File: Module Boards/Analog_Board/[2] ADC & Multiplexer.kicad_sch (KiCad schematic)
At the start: 10 parts, among them J1 212134-0003, J2 212134-0003, J3 212134-0003, J4 212134-0003, U1 LTC1864LIMS8#PBF, U5 TMUX1104DQAR

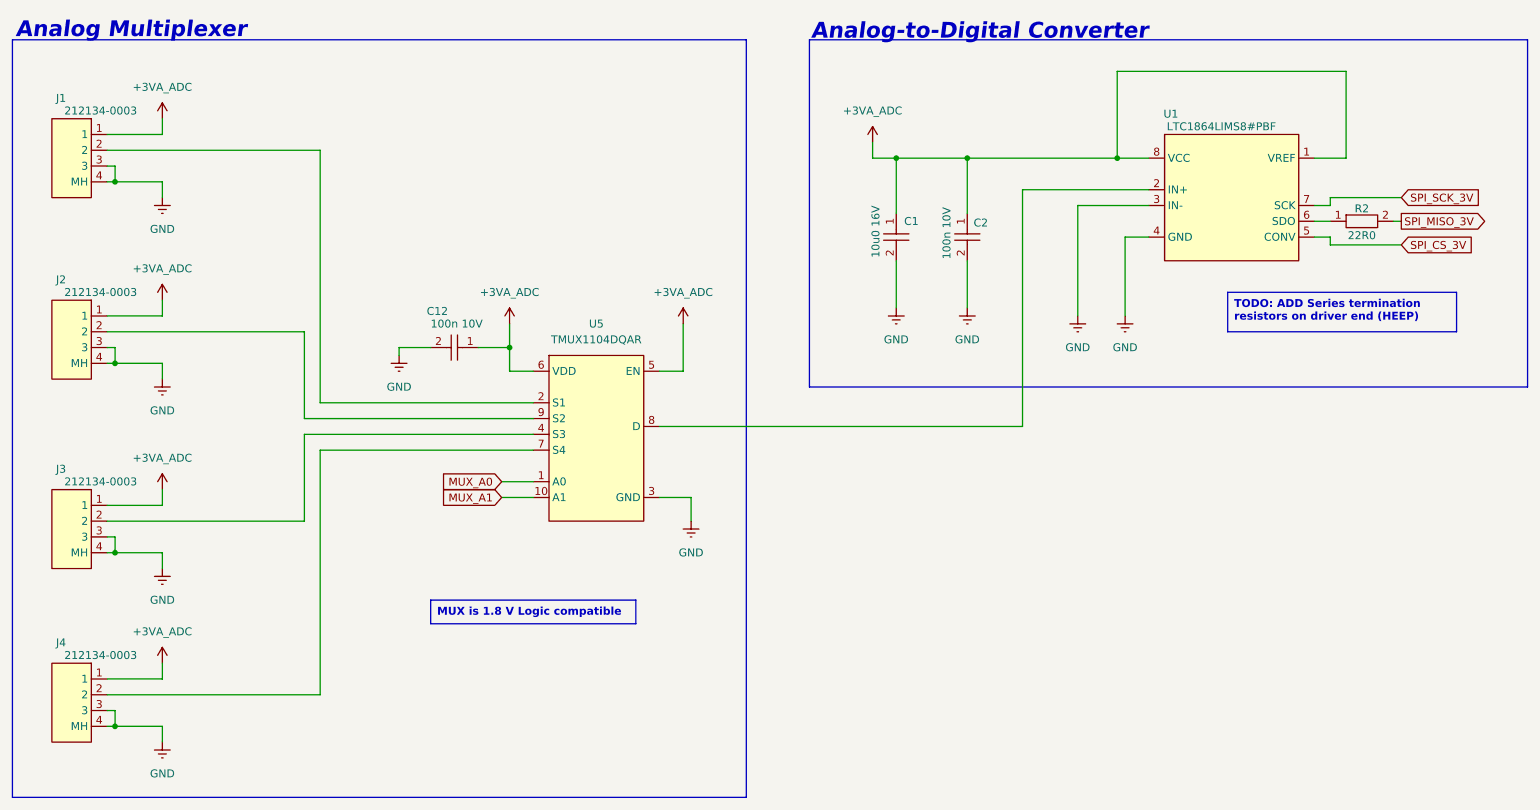
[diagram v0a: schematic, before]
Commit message: Routed Analog Board
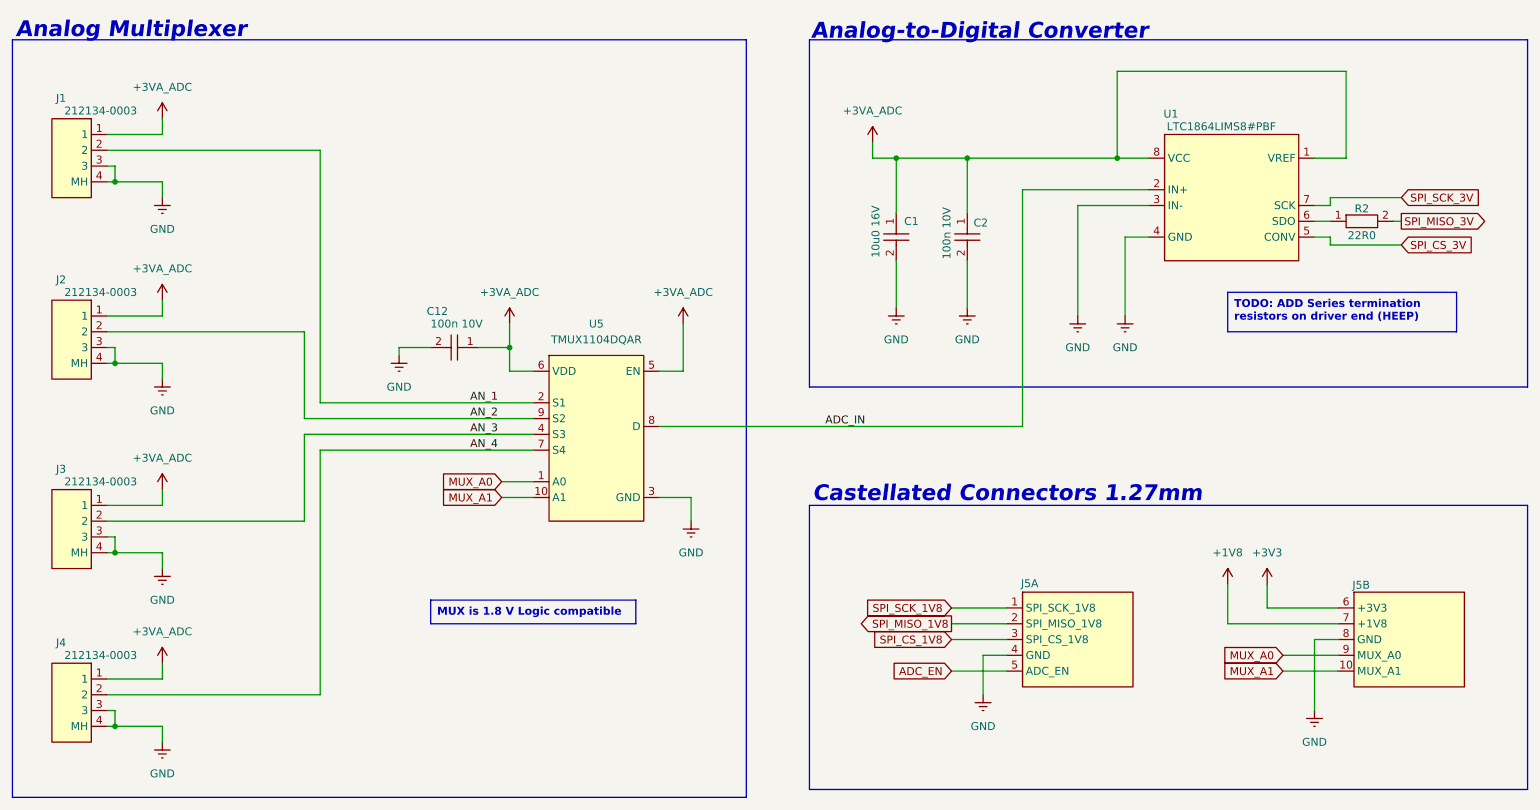
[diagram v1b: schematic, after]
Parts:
- added J5: ~, X-MODs_PcbLib:Analog_Board_Castellated_Conn_1.27mm, symbol X-MODs_SchLib:Analog_Board_Castellated_Conn_1.27mm
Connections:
- net GND: now also J5.4 (GND), J5.8 (GND)
- net MUX_A0: now also J5.9 (MUX_A0)
- net MUX_A1: now also J5.10 (MUX_A1)
- net AN_1: now reaches J1.2, U5.2 (S1)
- net AN_3: now reaches J3.2, U5.4 (S3)
- net AN_4: now reaches J4.2, U5.7 (S4)
- net ADC_IN: now reaches U1.2 (IN+), U5.8 (D)
- net AN_2: now reaches J2.2, U5.9 (S2)
- new net +1V8: J5.7 (+1V8)
- new net +3V3: J5.6 (+3V3)
- new net ADC_EN: J5.5 (ADC_EN)
- new net SPI_CS_1V8: J5.3 (SPI_CS_1V8)
- new net SPI_MISO_1V8: J5.2 (SPI_MISO_1V8)
- new net SPI_SCK_1V8: J5.1 (SPI_SCK_1V8)
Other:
- note added: "Castellated Connectors 1.27mm"
